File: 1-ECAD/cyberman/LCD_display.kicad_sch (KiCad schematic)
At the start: 1 part, among them J2 YXT-BB10-24S-02

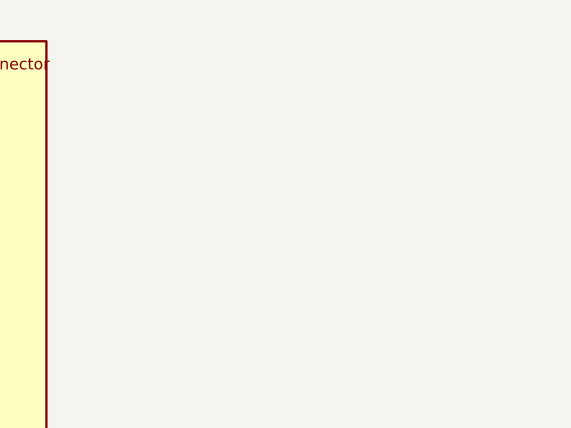
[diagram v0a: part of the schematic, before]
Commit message: add mic and speaker
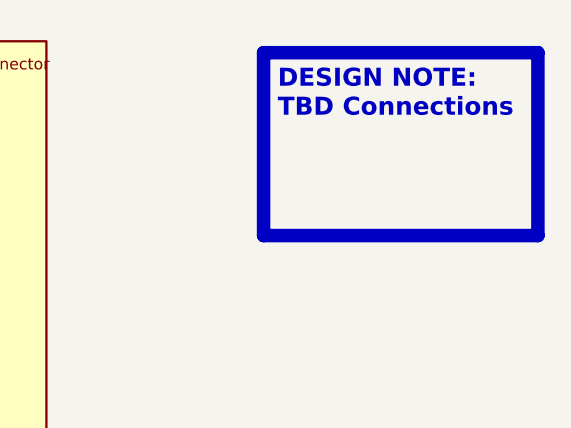
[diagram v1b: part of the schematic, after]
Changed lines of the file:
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@@
 	(generator_version "8.0")
 	(paper "A4")
+	(text_box "DESIGN NOTE:\nTBD Connections"
+		(exclude_from_sim no)
+		(at 189.23 39.37 0)
+		(size 30.48 20.32)
+		(stroke
+			(width 1.5)
+			(type solid)
+			(color 255 0 0 1)
+		)
+		(fill
+			(type none)
+		)
+		(effects
+			(font
+				(face "Times New Roman")
+				(size 2 2)
+				(thickness 0.4)
+				(bold yes)
+				(color 255 0 0 1)
+			)
+			(justify left top)
+		)
+	)
 	(symbol
 		(lib_id "0_connector_smd:YXT-BB10-24S-02")

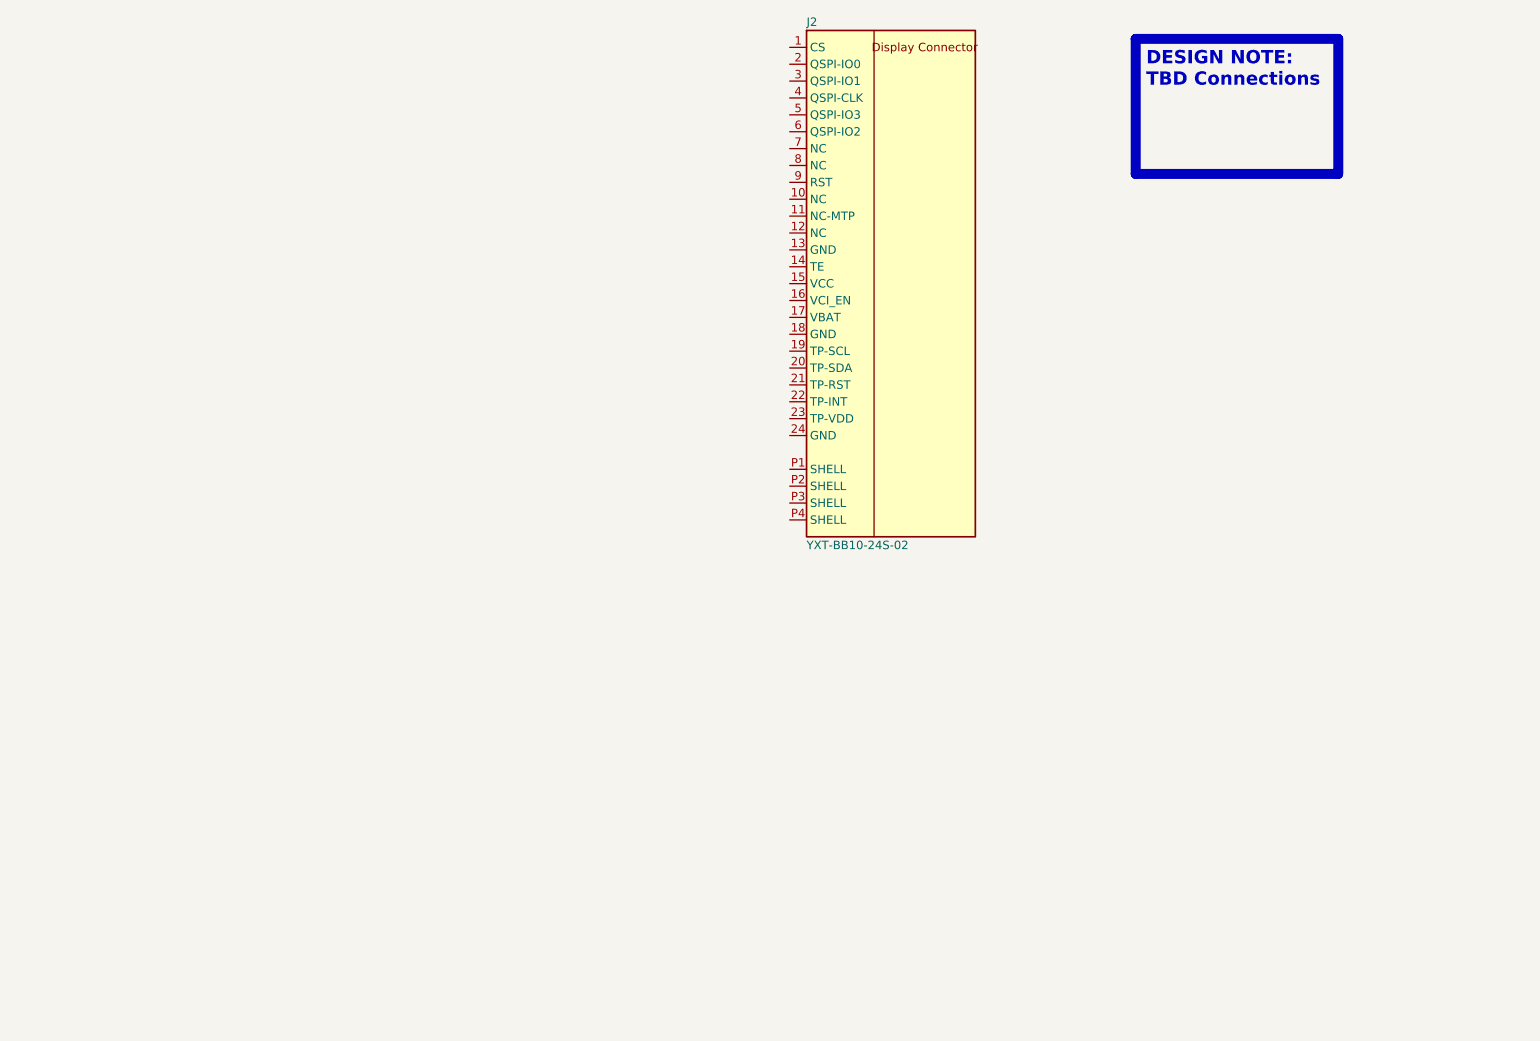
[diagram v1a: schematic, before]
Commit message: add bus and display connection
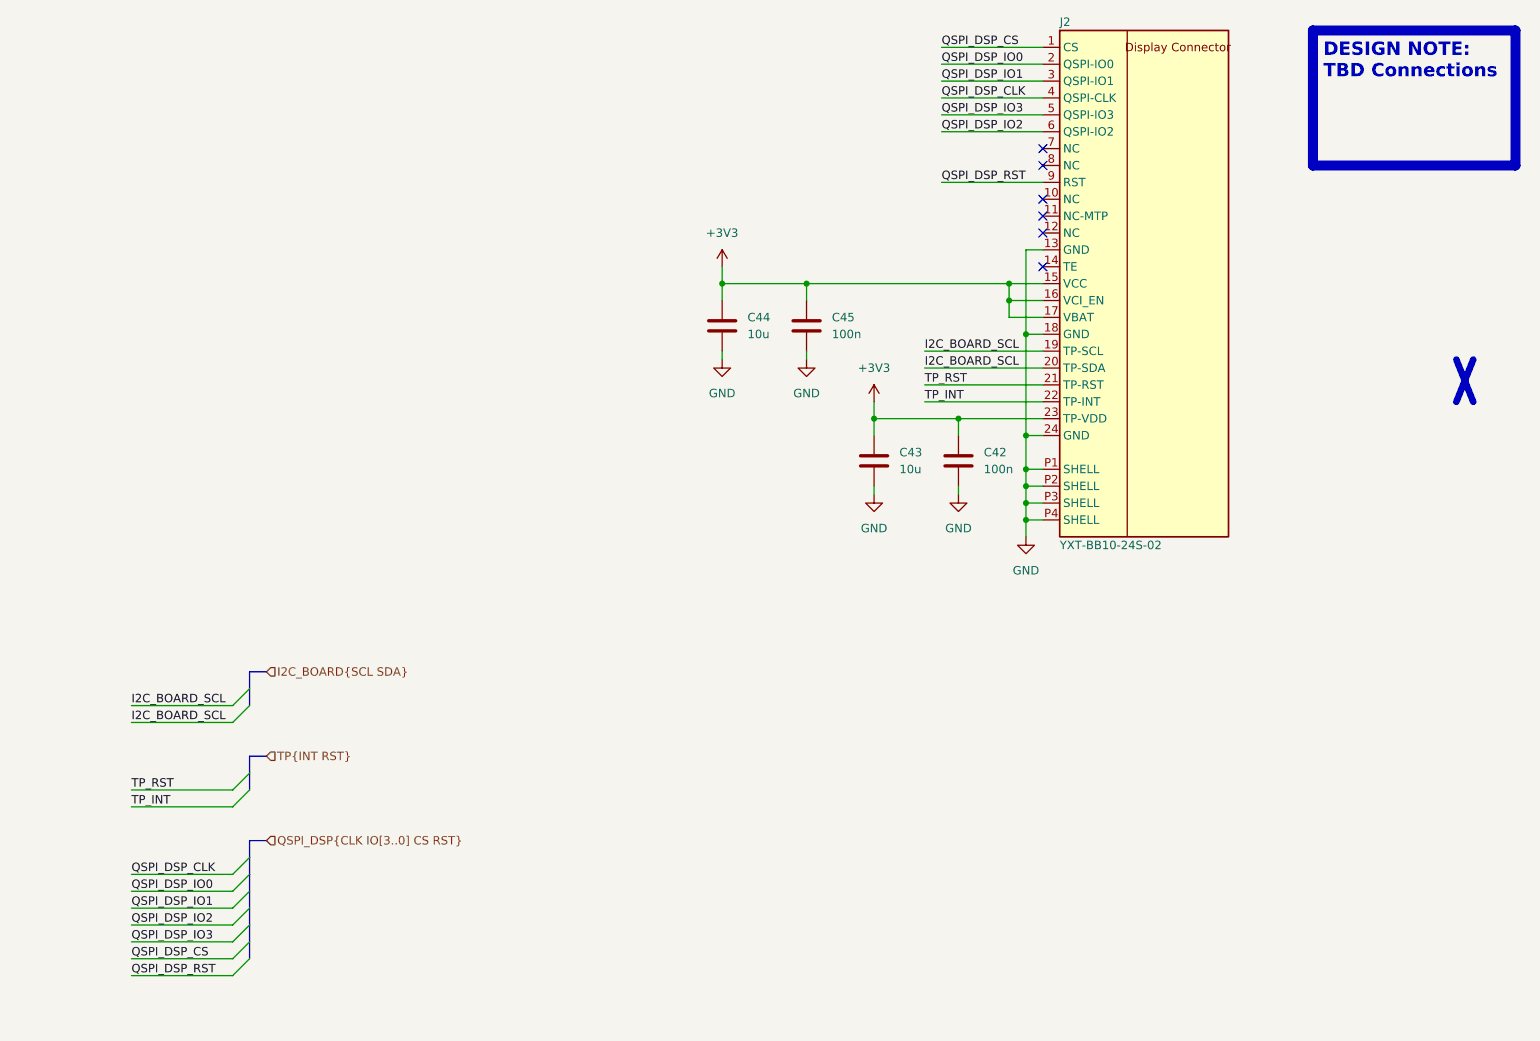
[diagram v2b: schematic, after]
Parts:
- added C42, C45: 100n, symbol Device:C
- added C43, C44: 10u, symbol Device:C
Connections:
- net QSPI_DSP_CS: now reaches J2.1 (CS)
- net GND: now reaches J2.13 (GND)
- net GND: now also J2.18 (GND), J2.24 (GND), J2.P1 (SHELL), J2.P2 (SHELL), J2.P3 (SHELL), J2.P4 (SHELL), C42.2, C43.2, C44.2, C45.2
- net +3V3: now reaches J2.15 (VCC)
- net +3V3: now also J2.16 (VCI_EN), J2.17 (VBAT), J2.23 (TP-VDD), C42.1, C43.1, C44.1, C45.1
- net I2C_BOARD_SCL: now reaches J2.19 (TP-SCL)
- net I2C_BOARD_SCL: now also J2.20 (TP-SDA)
- net QSPI_DSP_IO0: now reaches J2.2 (QSPI-IO0)
- net TP_RST: now reaches J2.21 (TP-RST)
- net TP_INT: now reaches J2.22 (TP-INT)
- net QSPI_DSP_IO1: now reaches J2.3 (QSPI-IO1)
- net QSPI_DSP_CLK: now reaches J2.4 (QSPI-CLK)
- net QSPI_DSP_IO3: now reaches J2.5 (QSPI-IO3)
- net QSPI_DSP_IO2: now reaches J2.6 (QSPI-IO2)
- net QSPI_DSP_RST: now reaches J2.9 (RST)
- no-connect marks 0 -> 6
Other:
- moved on the sheet: J2

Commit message: hey
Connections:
- net +3V3: no longer J2.17 (VBAT)
- net I2C_BOARD_SCL renamed BOARD_I2C.SCL
- net BOARD_I2C.SCL: no longer J2.20 (TP-SDA)
- net QSPI_DSP_CLK renamed QSPI.CLK
- net QSPI_DSP_CS renamed DSP.CS
- net QSPI_DSP_IO0 renamed QSPI.IO0
- net QSPI_DSP_IO1 renamed QSPI.IO1
- net QSPI_DSP_IO2 renamed QSPI.IO2
- net QSPI_DSP_IO3 renamed QSPI.IO3
- net QSPI_DSP_RST renamed DSP.RST
- net TP_INT renamed TP.INT
- net TP_RST renamed TP.RST
- new net +BATT: J2.17 (VBAT)
- new net BOARD_I2C.SDA: J2.20 (TP-SDA)
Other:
- note added: "MISO/IO1"
- note added: "MOSI/IO0"
- moved on the sheet: C44, C45

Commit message: connections
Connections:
- net TP.RST is gone; now on net DSP.RST: J2.21 (TP-RST)
- no-connect marks 6 -> 7

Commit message: footpritn day
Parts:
- J2: footprint (none) -> 0_connector_smd:YXT-BB10-24S-02

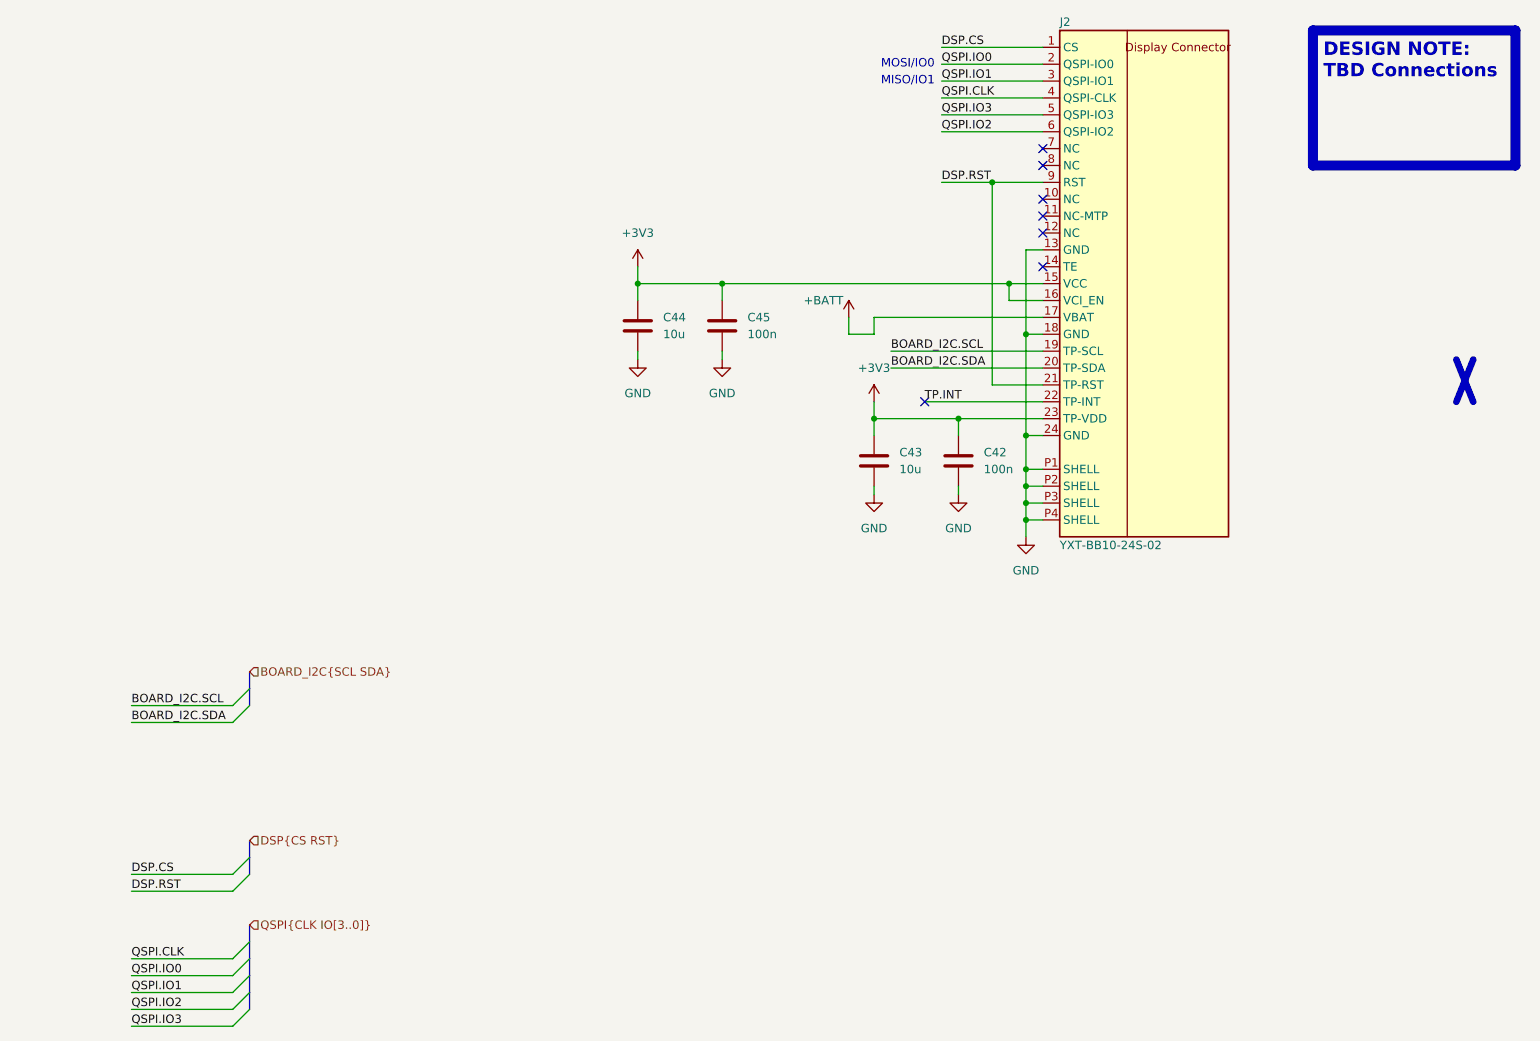
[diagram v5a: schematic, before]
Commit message: new changes
close display page and peripheral schematic
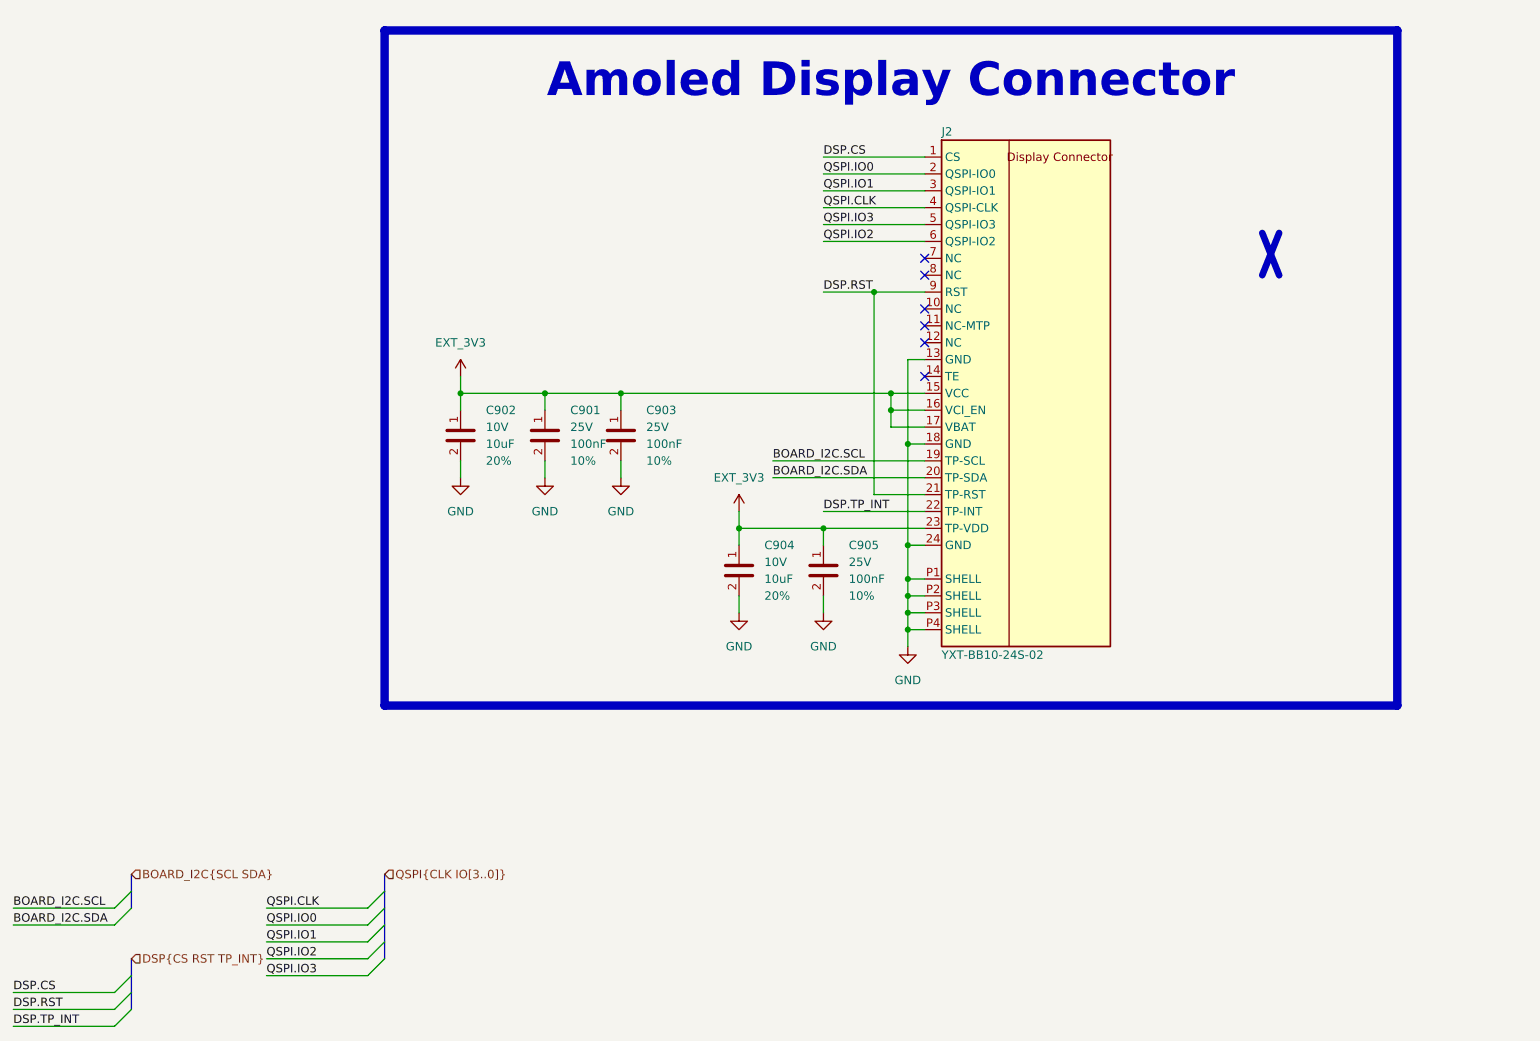
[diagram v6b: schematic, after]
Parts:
- removed C42, C45: 100n, symbol Device:C
- removed C43, C44: 10u, symbol Device:C
- added C901, C903, C905: CC0402KRX7R8BB104, 0_capacitor_smd:C_0402, symbol 0_capacitor_smd:CC0402KRX7R8BB104
- added C902, C904: CC0402MRX5R6BB106, 0_capacitor_smd:C_0402, symbol 0_capacitor_smd:CC0402MRX5R6BB106
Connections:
- net +BATT is gone; now on net EXT_3V3: J2.17 (VBAT)
- net GND: now also C901.2, C902.2, C903.2, C904.2, C905.2
- net +3V3 renamed EXT_3V3
- net EXT_3V3: now also C901.1, C902.1, C903.1, C904.1, C905.1
- net TP.INT renamed DSP.TP_INT
- no-connect marks 7 -> 6
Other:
- note added: "Amoled Display Connector"
- note removed: "MISO/IO1"
- note removed: "MOSI/IO0"
- company: (none) -> kode.
- title: (none) -> Amoled Display
- moved on the sheet: J2
